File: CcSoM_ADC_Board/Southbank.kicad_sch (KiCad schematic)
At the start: 1 part, among them J1 SoM Connector

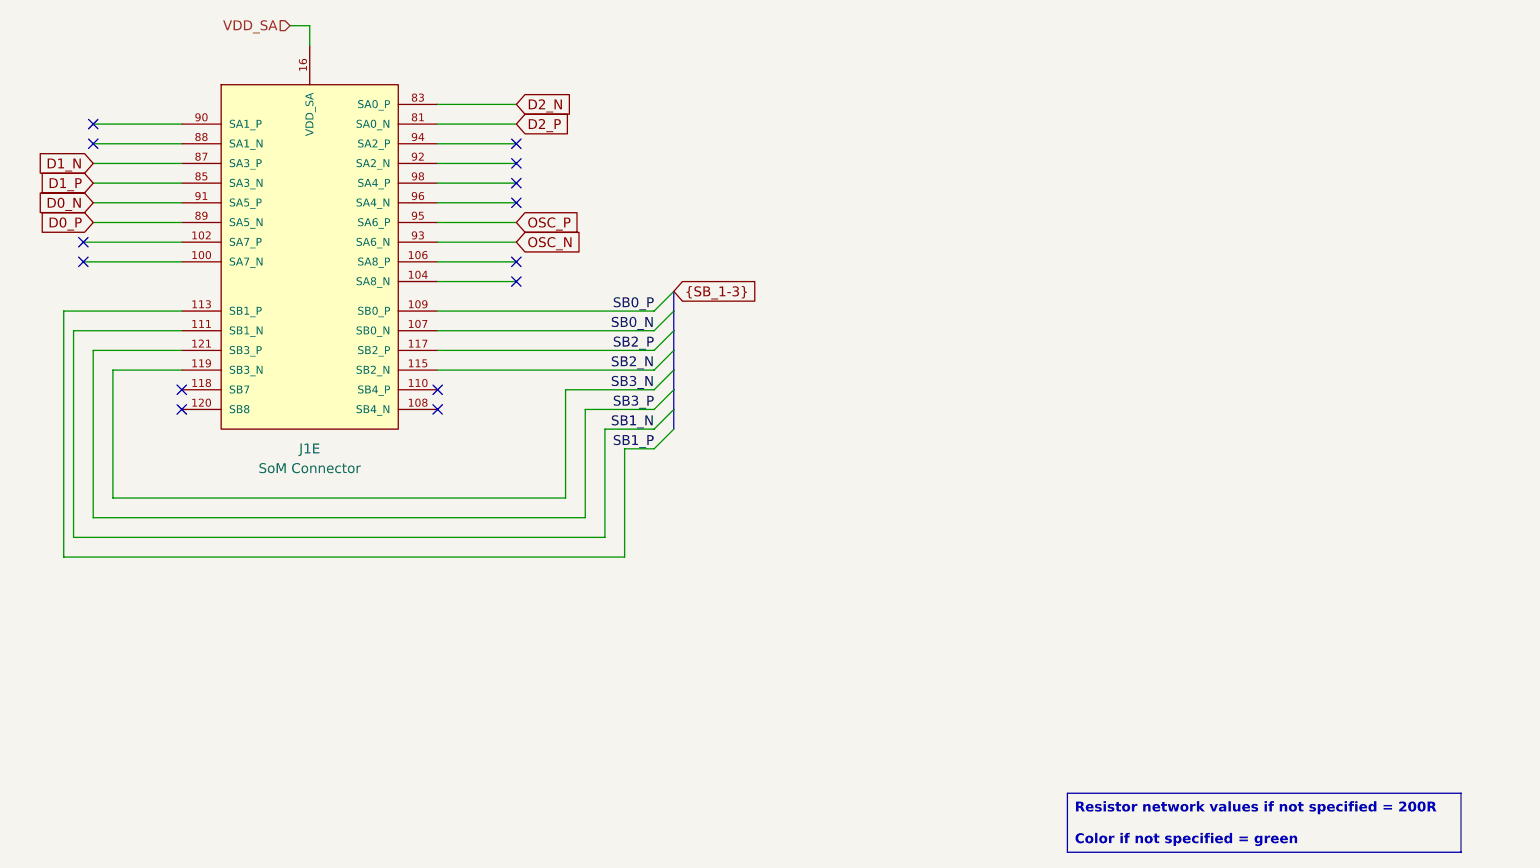
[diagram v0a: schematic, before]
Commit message: changed from 10Bit ADC to 12Bit
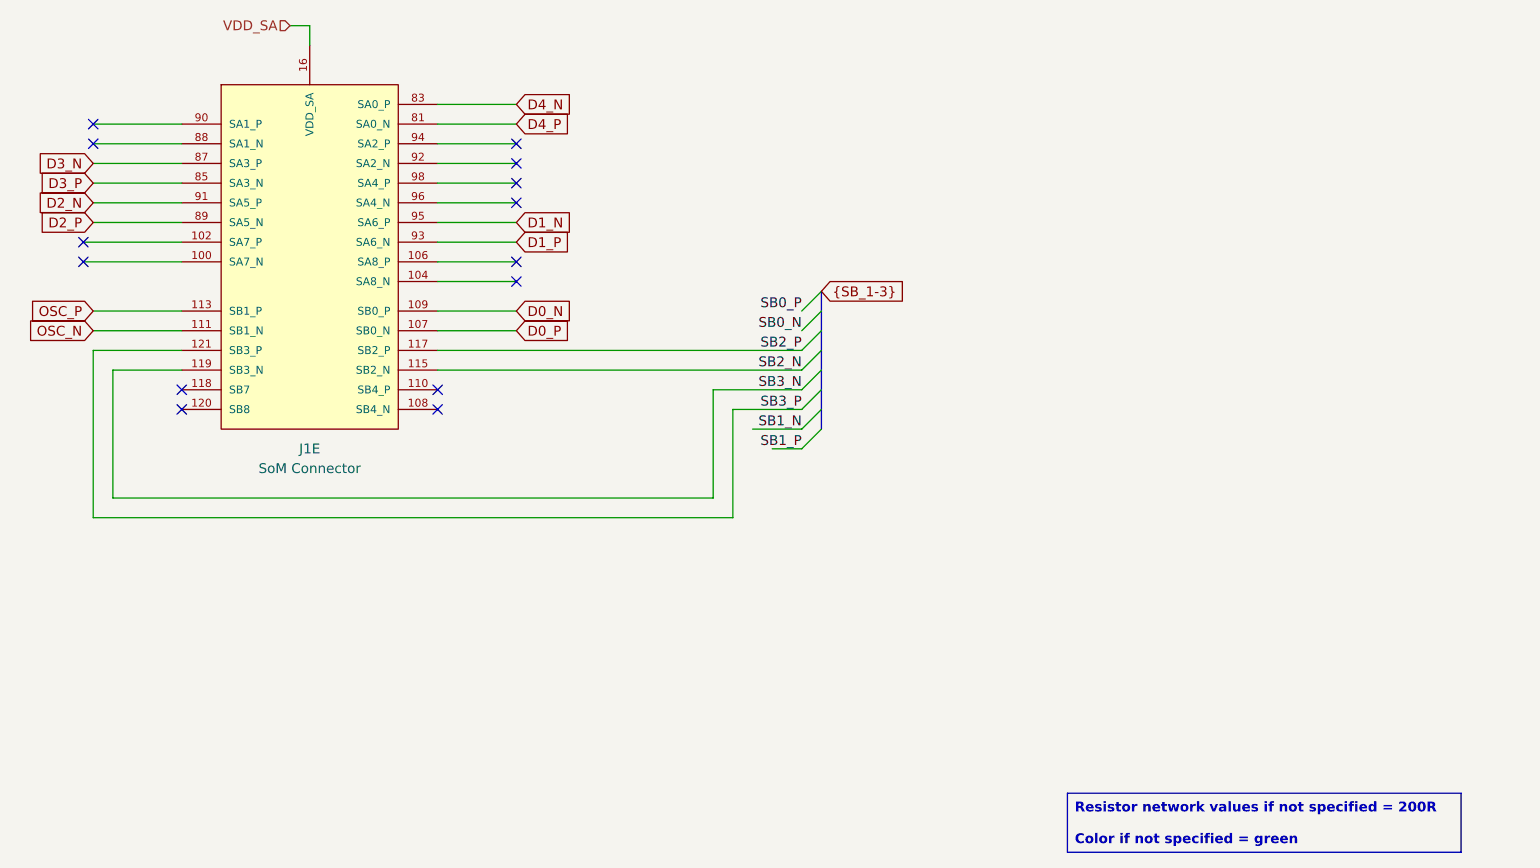
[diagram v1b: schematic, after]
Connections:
- net D0_N: now also J1.109 (SB0_P); no longer J1.91 (SA5_P)
- net D0_P: now also J1.107 (SB0_N); no longer J1.89 (SA5_N)
- net D1_N: now also J1.95 (SA6_P); no longer J1.87 (SA3_P)
- net D1_P: now also J1.93 (SA6_N); no longer J1.85 (SA3_N)
- net D2_N: now also J1.91 (SA5_P); no longer J1.83 (SA0_P)
- net D2_P: now also J1.89 (SA5_N); no longer J1.81 (SA0_N)
- net OSC_N: now also J1.111 (SB1_N); no longer J1.93 (SA6_N)
- net OSC_P: now also J1.113 (SB1_P); no longer J1.95 (SA6_P)
- net SB0_N: no longer J1.107 (SB0_N)
- net SB0_P: no longer J1.109 (SB0_P)
- net SB1_N: no longer J1.111 (SB1_N)
- net SB1_P: no longer J1.113 (SB1_P)
- new net D3_N: J1.87 (SA3_P)
- new net D3_P: J1.85 (SA3_N)
- new net D4_N: J1.83 (SA0_P)
- new net D4_P: J1.81 (SA0_N)

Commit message: corrected schematic created pdf and bom file
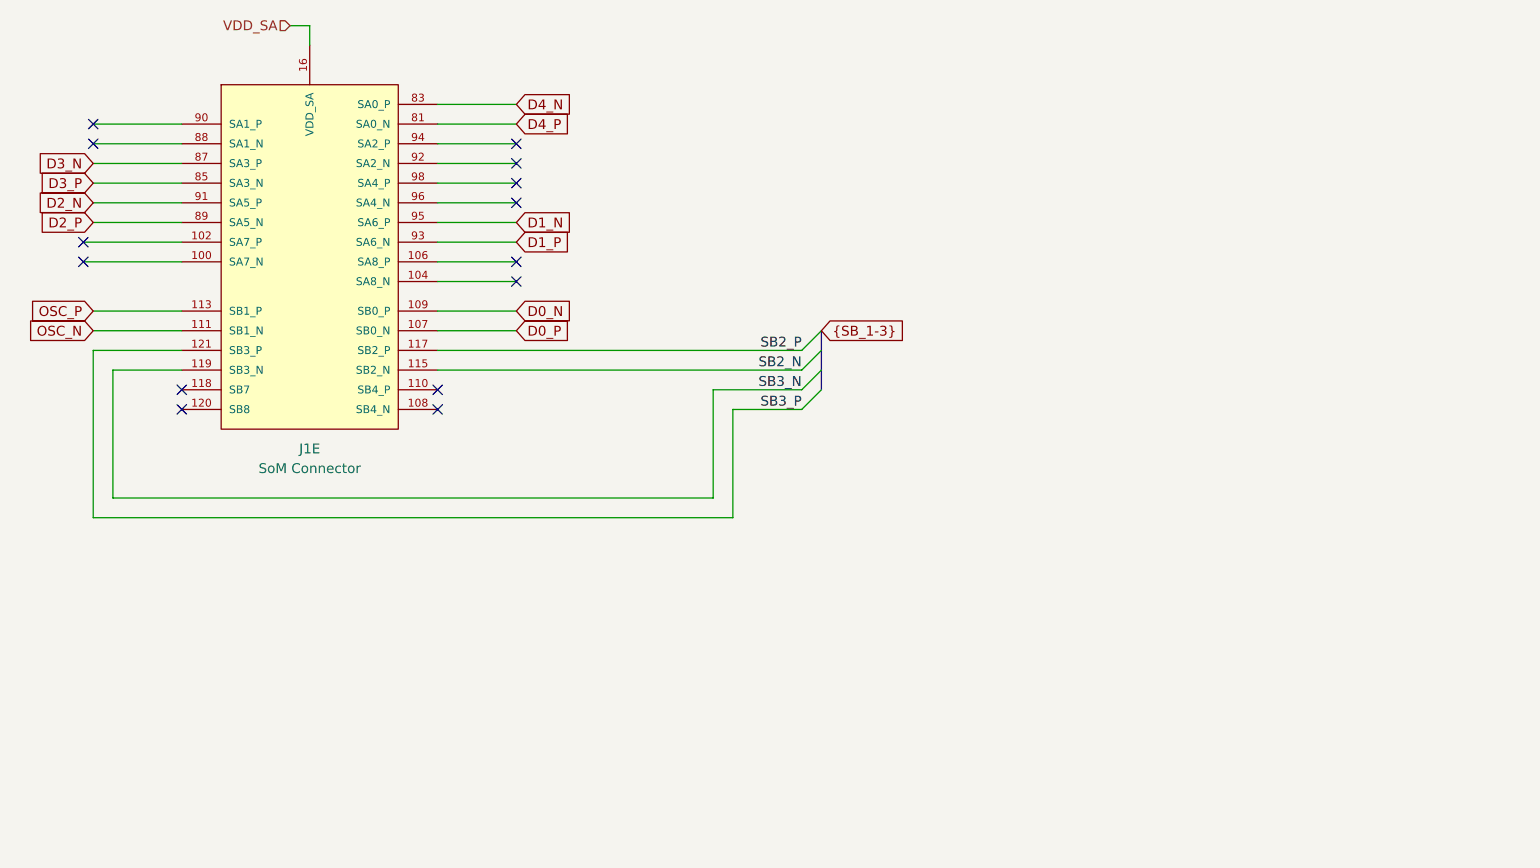
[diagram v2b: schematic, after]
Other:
- title: SoM Programmer & Tester -> SoM Programmer & ADC Board

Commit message: digikey no not complete
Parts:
- J1: DigiKey_no (none) -> A121565-ND
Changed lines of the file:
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@@
+			)
+		)
+		(property "DigiKey_no" "A121565-ND"
+			(at 135.89 73.66 0)
+			(effects
+				(font
+					(size 1.27 1.27)
+				)
+				(hide yes)
 			)
 		)
